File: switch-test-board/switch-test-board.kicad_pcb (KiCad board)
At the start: 4 copper layers, 1 part, among them U1 RPI4CM

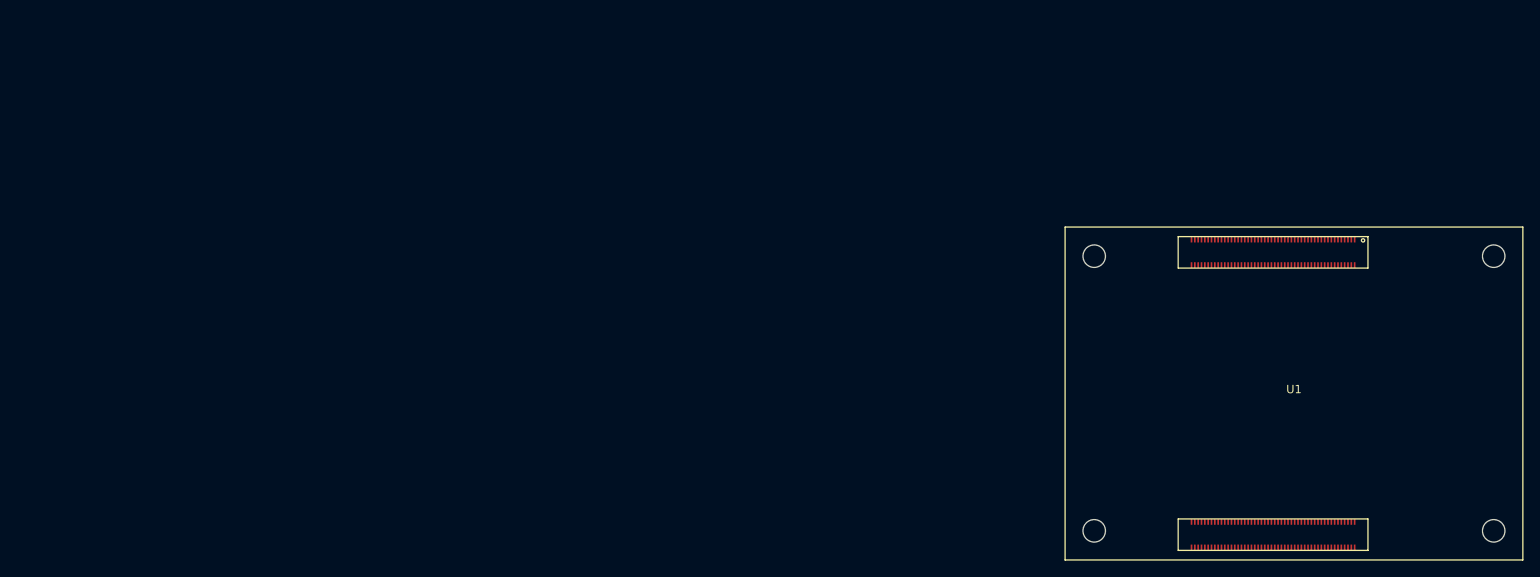
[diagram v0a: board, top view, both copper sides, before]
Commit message: Added KSZ Switch IC Decoupling and Port Leds.
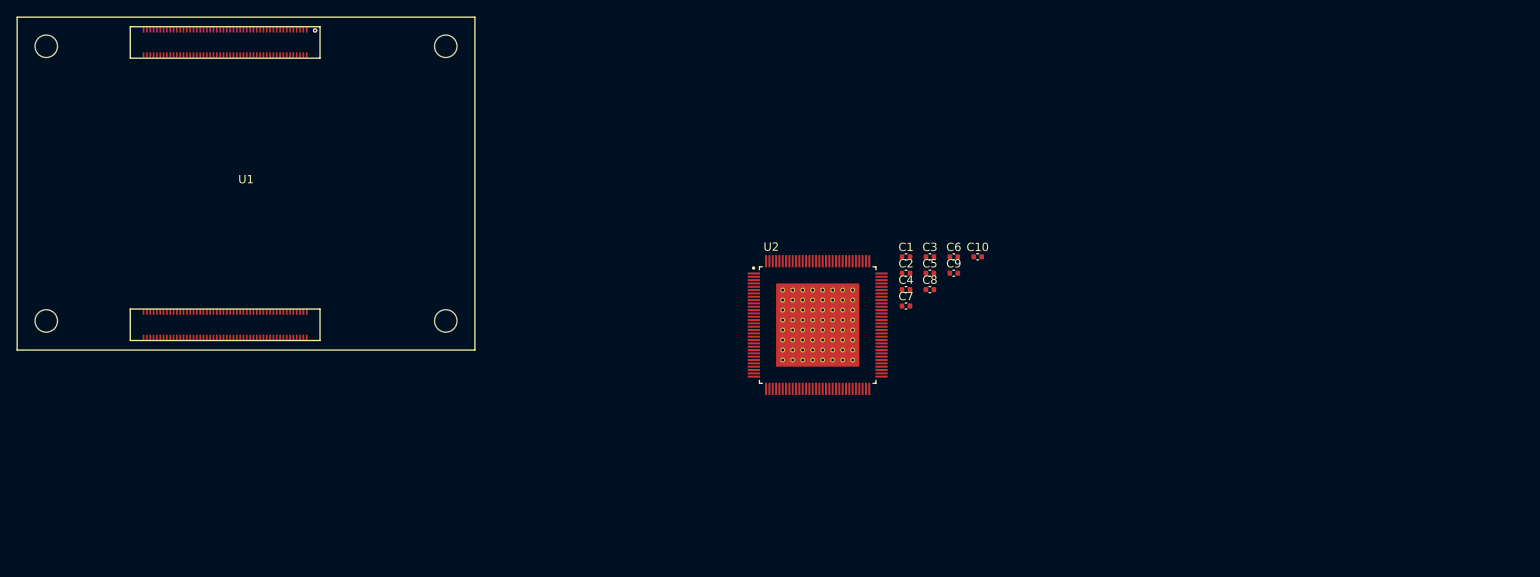
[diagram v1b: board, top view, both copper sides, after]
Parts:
- added C1: 1uF, Capacitor_SMD:C_0402_1005Metric, F.Cu at (153.4, 59.3)
- added C10: 0.1uF, Capacitor_SMD:C_0402_1005Metric, F.Cu at (162.0, 59.3)
- added C2: 0.1uF, Capacitor_SMD:C_0402_1005Metric, F.Cu at (153.4, 61.3)
- added C3: 0.1uF, Capacitor_SMD:C_0402_1005Metric, F.Cu at (156.3, 59.3)
- added C4: 0.1uF, Capacitor_SMD:C_0402_1005Metric, F.Cu at (153.4, 63.2)
- added C5: 0.1uF, Capacitor_SMD:C_0402_1005Metric, F.Cu at (156.3, 61.3)
- added C6: 0.1uF, Capacitor_SMD:C_0402_1005Metric, F.Cu at (159.1, 59.3)
- added C7: 0.1uF, Capacitor_SMD:C_0402_1005Metric, F.Cu at (153.4, 65.2)
- added C8: 0.1uF, Capacitor_SMD:C_0402_1005Metric, F.Cu at (156.3, 63.2)
- added C9: 0.1uF, Capacitor_SMD:C_0402_1005Metric, F.Cu at (159.1, 61.3)
- added U2: KSZ9477S, kicad-lib:128-TQFP-EP, F.Cu at (142.8, 67.5)
- moved U1 128.4 mm to (46.6, 70.5)
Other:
- net class Default: clearance 0.2 -> 0.15
- rule pad_to_mask_clearance: 0 -> 0.07
- rule trace_clearance: 0.2 -> 0.15

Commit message: Updated Schematic.
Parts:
- added C1: 15pF, Capacitor_SMD:C_0402_1005Metric, F.Cu at (132.6, 63.8)
- added C10: 10uF, Capacitor_SMD:C_0603_1608Metric, F.Cu at (150.5, 49.6)
- added C12: 1uF, Capacitor_SMD:C_0402_1005Metric, F.Cu at (160.3, 52.5)
- added C14: 0.1uF, Capacitor_SMD:C_0402_1005Metric, F.Cu at (123.9, 59.8)
- added C16: 0.1uF, Capacitor_SMD:C_0402_1005Metric, F.Cu at (149.8, 61.8)
- added C18: 0.1uF, Capacitor_SMD:C_0402_1005Metric, F.Cu at (157.4, 54.5)
- added C19: 0.1uF, Capacitor_SMD:C_0402_1005Metric, F.Cu at (173.3, 38.2)
- added C2: 15pF, Capacitor_SMD:C_0402_1005Metric, F.Cu at (153.1, 55.8)
- added C21: 0.1uF, Capacitor_SMD:C_0402_1005Metric, F.Cu at (146.9, 64.1)
- added C22: 0.1uF, Capacitor_SMD:C_0402_1005Metric, F.Cu at (151.2, 59.8)
- added C24: 0.1uF, Capacitor_SMD:C_0402_1005Metric, F.Cu at (161.8, 49.4)
- added C25: 0.1uF, Capacitor_SMD:C_0402_1005Metric, F.Cu at (157.4, 52.5)
- added C27: 0.1uF, Capacitor_SMD:C_0402_1005Metric, F.Cu at (153.1, 57.8)
- added C28: 0.1uF, Capacitor_SMD:C_0402_1005Metric, F.Cu at (146.9, 62.2)
- added C3: 10uF, Capacitor_SMD:C_0603_1608Metric, F.Cu at (146.5, 49.6)
- added C30: 0.1uF, Capacitor_SMD:C_0402_1005Metric, F.Cu at (173.3, 36.2)
- added C31: 0.1uF, Capacitor_SMD:C_0402_1005Metric, F.Cu at (125.6, 64.2)
- added C33: 0.1uF, Capacitor_SMD:C_0402_1005Metric, F.Cu at (138.3, 62.2)
- added C34: 0.1uF, Capacitor_SMD:C_0402_1005Metric, F.Cu at (122.7, 64.2)
- added C36: 0.1uF, Capacitor_SMD:C_0402_1005Metric, F.Cu at (144.1, 64.1)
- added C37: 0.1uF, Capacitor_SMD:C_0402_1005Metric, F.Cu at (141.2, 64.1)
- added C38: 0.1uF, Capacitor_SMD:C_0402_1005Metric, F.Cu at (138.3, 64.1)
- added C39: 0.1uF, Capacitor_SMD:C_0402_1005Metric, F.Cu at (135.5, 64.1)
- added C4: 10uF, Capacitor_SMD:C_0603_1608Metric, F.Cu at (142.4, 49.6)
- added C40: 0.1uF, Capacitor_SMD:C_0402_1005Metric, F.Cu at (144.1, 62.2)
- added C41: 0.1uF, Capacitor_SMD:C_0402_1005Metric, F.Cu at (141.2, 62.2)
- added C42: 0.1uF, Capacitor_SMD:C_0402_1005Metric, F.Cu at (129.7, 63.8)
- added C43: 0.1uF, Capacitor_SMD:C_0402_1005Metric, F.Cu at (135.5, 62.2)
- added C44: 0.1uF, Capacitor_SMD:C_0402_1005Metric, F.Cu at (148.3, 59.8)
- added C45: 10uF, Capacitor_SMD:C_0603_1608Metric, F.Cu at (168.5, 74.7)
- added C46: 0.1uF, Capacitor_SMD:C_0402_1005Metric, F.Cu at (179.0, 74.4)
- added C47: 10uF, Capacitor_SMD:C_0603_1608Metric, F.Cu at (168.5, 77.2)
- added C48: 0.1uF, Capacitor_SMD:C_0402_1005Metric, F.Cu at (178.4, 77.5)
- added C49: 10uF, Capacitor_SMD:C_0603_1608Metric, F.Cu at (172.5, 74.7)
- added C5: 10uF, Capacitor_SMD:C_0603_1608Metric, F.Cu at (130.4, 52.2)
- added C50: 0.1uF, Capacitor_SMD:C_0402_1005Metric, F.Cu at (177.3, 79.5)
- added C6: 10uF, Capacitor_SMD:C_0603_1608Metric, F.Cu at (126.3, 54.8)
- added C7: 10uF, Capacitor_SMD:C_0603_1608Metric, F.Cu at (134.4, 49.6)
- added C8: 10uF, Capacitor_SMD:C_0603_1608Metric, F.Cu at (138.4, 49.6)
- added C9: 10uF, Capacitor_SMD:C_0603_1608Metric, F.Cu at (154.5, 49.6)
- added D1: 150060GS75000, LED_SMD:LED_0603_1608Metric, F.Cu at (126.4, 49.7)
- added D10: 150060RS75000, LED_SMD:LED_0603_1608Metric, F.Cu at (173.9, 31.4)
- added D2: 150060GS75000, LED_SMD:LED_0603_1608Metric, F.Cu at (115.2, 63.3)
- added D3: 150060GS75000, LED_SMD:LED_0603_1608Metric, F.Cu at (119.3, 63.3)
- added D4: 150060GS75000, LED_SMD:LED_0603_1608Metric, F.Cu at (124.5, 57.5)
- added D5: 150060GS75000, LED_SMD:LED_0603_1608Metric, F.Cu at (120.5, 60.1)
- added D6: 150060RS75000, LED_SMD:LED_0603_1608Metric, F.Cu at (120.5, 57.5)
- added D7: 150060RS75000, LED_SMD:LED_0603_1608Metric, F.Cu at (173.9, 33.9)
- added D8: 150060RS75000, LED_SMD:LED_0603_1608Metric, F.Cu at (126.4, 52.2)
- added D9: 150060RS75000, LED_SMD:LED_0603_1608Metric, F.Cu at (130.4, 49.7)
- added FB1: BLM18EG221SN1D, kicad-lib:ferrite-blm18, F.Cu at (134.2, 52.0)
- added FB2: BLM18EG221SN1D, kicad-lib:ferrite-blm18, F.Cu at (137.8, 52.0)
- added FB3: BLM18EG221SN1D, kicad-lib:ferrite-blm18, F.Cu at (141.3, 52.0)
- added FB4: BLM18EG221SN1D, kicad-lib:ferrite-blm18, F.Cu at (144.8, 52.0)
- added FB5: BLM18EG221SN1D, kicad-lib:ferrite-blm18, F.Cu at (148.4, 52.0)
- added FB6: BLM18EG221SN1D, kicad-lib:ferrite-blm18, F.Cu at (168.3, 79.6)
- added FB7: BLM18EG221SN1D, kicad-lib:ferrite-blm18, F.Cu at (172.3, 77.1)
- added J1: 1367073-1, kicad-lib:SFP_with_Cage, F.Cu at (162.9, 39.2)
- added J3: 2011-2X10G00SD025B, Connector_PinHeader_2.54mm:PinHeader_2x10_P2.54mm_Vertical, F.Cu at (167.0, 32.4)
- added R1: 6.04K %1, Resistor_SMD:R_0402_1005Metric, F.Cu at (138.5, 56.2)
- added R10: 10K_DNP, Resistor_SMD:R_0402_1005Metric, F.Cu at (133.8, 58.2)
- added R11: 4.7K, Resistor_SMD:R_0402_1005Metric, F.Cu at (136.7, 58.2)
- added R12: 10K, Resistor_SMD:R_0402_1005Metric, F.Cu at (139.6, 58.2)
- added R13: 10K, Resistor_SMD:R_0402_1005Metric, F.Cu at (142.5, 58.2)
- added R14: 10K, Resistor_SMD:R_0402_1005Metric, F.Cu at (145.4, 58.2)
- added R15: 10K, Resistor_SMD:R_0402_1005Metric, F.Cu at (133.8, 60.2)
- added R16: 10K, Resistor_SMD:R_0402_1005Metric, F.Cu at (151.6, 51.9)
- added R17: 1K, Resistor_SMD:R_0402_1005Metric, F.Cu at (150.2, 55.9)
- added R18: 1K, Resistor_SMD:R_0402_1005Metric, F.Cu at (154.5, 51.9)
- added R19: 1K, Resistor_SMD:R_0402_1005Metric, F.Cu at (151.6, 53.9)
- added R2: 191 %1, Resistor_SMD:R_0402_1005Metric, F.Cu at (141.4, 56.2)
- added R20: 1K, Resistor_SMD:R_0402_1005Metric, F.Cu at (154.5, 53.9)
- added R21: 1K, Resistor_SMD:R_0402_1005Metric, F.Cu at (129.8, 55.9)
- added R22: 1K, Resistor_SMD:R_0402_1005Metric, F.Cu at (132.7, 54.5)
- added R23: 1K, Resistor_SMD:R_0402_1005Metric, F.Cu at (135.6, 54.2)
- added R24: 1K, Resistor_SMD:R_0402_1005Metric, F.Cu at (138.5, 54.2)
- added R25: 1K, Resistor_SMD:R_0402_1005Metric, F.Cu at (141.4, 54.2)
- added R26: 1K, Resistor_SMD:R_0402_1005Metric, F.Cu at (129.8, 61.8)
- added R27: 4.7K, Resistor_SMD:R_0402_1005Metric, F.Cu at (130.9, 57.8)
- added R28: 750R, Resistor_SMD:R_0402_1005Metric, F.Cu at (135.6, 56.2)
- added R29: 750R, Resistor_SMD:R_0402_1005Metric, F.Cu at (126.8, 62.2)
- added R3: 22R, Resistor_SMD:R_0402_1005Metric, F.Cu at (144.3, 56.2)
- added R30: 750R, Resistor_SMD:R_0402_1005Metric, F.Cu at (126.8, 60.2)
- added R31: 750R, Resistor_SMD:R_0402_1005Metric, F.Cu at (139.6, 60.2)
- added R32: 750R, Resistor_SMD:R_0402_1005Metric, F.Cu at (142.5, 60.2)
- added R33: 750R, Resistor_SMD:R_0402_1005Metric, F.Cu at (145.4, 60.2)
- added R34: 750R, Resistor_SMD:R_0402_1005Metric, F.Cu at (123.9, 62.2)
- added R35: 22R, Resistor_SMD:R_0402_1005Metric, F.Cu at (147.2, 54.2)
- added R36: 1K, Resistor_SMD:R_0402_1005Metric, F.Cu at (171.5, 79.5)
- added R37: 10K, Resistor_SMD:R_0402_1005Metric, F.Cu at (175.5, 77.5)
- added R38: 10K, Resistor_SMD:R_0402_1005Metric, F.Cu at (174.4, 79.5)
- added R4: 22R, Resistor_SMD:R_0402_1005Metric, F.Cu at (147.2, 56.2)
- added R5: 22R, Resistor_SMD:R_0402_1005Metric, F.Cu at (136.7, 60.2)
- added R6: 22R, Resistor_SMD:R_0402_1005Metric, F.Cu at (150.2, 57.8)
- added R7: 22R, Resistor_SMD:R_0402_1005Metric, F.Cu at (128.0, 58.2)
- added R8: 22R, Resistor_SMD:R_0402_1005Metric, F.Cu at (144.3, 54.2)
- added R9: 22R, Resistor_SMD:R_0402_1005Metric, F.Cu at (130.9, 59.8)
- added SW1: PTS645SM43SMTR92 LFS, Button_Switch_SMD:SW_SPST_PTS645, F.Cu at (113.0, 52.3)
- added TP1: TestPoint_Small, TestPoint:TestPoint_Pad_D1.0mm, F.Cu at (176.0, 75.0)
- added U3: MIC826TYMT, Package_DFN_QFN:MLF-6-1EP_1.6x1.6mm_P0.5mm_EP0.5x1.26mm, F.Cu at (158.4, 49.9)
- added Y1: ABM8G-25.000MHZ-B4Y-T, Crystal:Crystal_SMD_Abracon_ABM8G-4Pin_3.2x2.5mm, F.Cu at (115.8, 59.8)
- moved C15 20.3 mm to (147.2, 77.5)
- moved C20 20.3 mm to (147.2, 79.5)
- moved C29 20.3 mm to (147.2, 81.4)
- moved C11 20.3 mm to (144.3, 77.5)
- moved C23 20.3 mm to (150.0, 77.5)
- moved C26 20.3 mm to (144.3, 83.4)
- moved C35 20.3 mm to (152.9, 77.5)
- moved C13 20.3 mm to (144.3, 79.5)
- moved C17 20.3 mm to (144.3, 81.4)
- moved C32 20.3 mm to (150.0, 79.5)
- moved U2 20.3 mm to (133.7, 85.7)
- renumbered C1 to C11, C2 to C13, C3 to C15, C4 to C17, C5 to C20, C6 to C23, C7 to C26, C8 to C29, C9 to C32, C10 to C35
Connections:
- net /VDDIO_3V3 renamed +3V3
- net Net-(U2-Pad101) renamed /SCLK
- net Net-(U2-Pad12) renamed /P2_TXRX_A_P
- net Net-(U2-Pad13) renamed /P2_TXRX_A_M
- net Net-(U2-Pad15) renamed /P2_TXRX_B_P
- net Net-(U2-Pad16) renamed /P2_TXRX_B_M
- net Net-(U2-Pad17) renamed /P2_TXRX_C_P
- net Net-(U2-Pad18) renamed /P2_TXRX_C_M
- net Net-(U2-Pad20) renamed /P2_TXRX_D_P
- net Net-(U2-Pad21) renamed /P2_TXRX_D_M
- net Net-(U2-Pad48) renamed /GTXCK
- net Net-(U2-Pad49) renamed /GTXCTL
- net Net-(U2-Pad52) renamed /GTXD3
- net Net-(U2-Pad53) renamed /GTXD2
- net Net-(U2-Pad54) renamed /GTXD1
- net Net-(U2-Pad55) renamed /GTXD0
- net Net-(U2-Pad93) renamed /PME_N
- net Net-(U2-Pad94) renamed /INTRP_N
- C11 pad 1: Net-(C1-Pad1) (its old number) -> /AVDDL_1V2
- C11 pad 2: Net-(C1-Pad2) -> GND
- C13 pad 1: Net-(C2-Pad1) (its old number) -> /AVDDL_1V2
- C13 pad 2: Net-(C2-Pad2) -> GND
- C15 pad 1: Net-(C3-Pad1) -> /AVDDL_1V2
- C15 pad 2: Net-(C3-Pad2) -> GND
- C17 pad 1: Net-(C4-Pad1) -> /AVDDL_1V2
- C17 pad 2: Net-(C4-Pad2) -> GND
- C20 pad 1: Net-(C5-Pad1) -> /AVDDL_1V2
- C20 pad 2: Net-(C5-Pad2) -> GND
- C23 pad 1: Net-(C6-Pad1) -> /AVDDL_1V2
- C23 pad 2: Net-(C6-Pad2) -> GND
- C26 pad 1: Net-(C7-Pad1) -> /AVDDL_1V2
- C26 pad 2: Net-(C7-Pad2) -> GND
- C29 pad 1: Net-(C8-Pad1) -> /AVDDL_1V2
- C29 pad 2: Net-(C8-Pad2) -> GND
- C32 pad 1: Net-(C9-Pad1) -> /AVDDL_1V2
- C32 pad 2: Net-(C9-Pad2) -> GND
- C35 pad 1: Net-(C10-Pad1) -> /AVDDL_1V2
- C35 pad 2: Net-(C10-Pad2) -> GND
- U2 pad 1: Net-(U2-Pad1) -> /P1_TXRX_A_P
- U2 pad 100: Net-(U2-Pad100) -> /SCS
- U2 pad 102: Net-(U2-Pad102) -> /LED5_0
- U2 pad 103: Net-(U2-Pad103) -> /LED5_1
- U2 pad 105: Net-(U2-Pad105) -> /LED1_0
- U2 pad 106: Net-(U2-Pad106) -> /LED1_1
- U2 pad 2: Net-(U2-Pad2) -> /P1_TXRX_A_M
- U2 pad 24: Net-(U2-Pad24) -> /P1_TXRX_A_M
- U2 pad 25: Net-(U2-Pad25) -> /P1_TXRX_A_P
- U2 pad 26: Net-(U2-Pad26) -> /P1_TXRX_B_P
- U2 pad 27: Net-(U2-Pad27) -> /P1_TXRX_B_M
- U2 pad 28: Net-(U2-Pad28) -> /P1_TXRX_C_P
- U2 pad 29: Net-(U2-Pad29) -> /P1_TXRX_C_M
- U2 pad 31: Net-(U2-Pad31) -> /P1_TXRX_D_P
- U2 pad 32: Net-(U2-Pad32) -> /P1_TXRX_D_M
- U2 pad 4: Net-(U2-Pad4) -> /P1_TXRX_B_P
- U2 pad 5: Net-(U2-Pad5) -> /P1_TXRX_B_M
- U2 pad 6: Net-(U2-Pad6) -> /P1_TXRX_C_P
- U2 pad 67: Net-(U2-Pad67) -> /IBA_EN
- U2 pad 7: Net-(U2-Pad7) -> /P1_TXRX_C_M
- U2 pad 78: Net-(U2-Pad78) -> /S_TX7_M
- U2 pad 79: Net-(U2-Pad79) -> /S_TX7_P
- U2 pad 8: Net-(U2-Pad8) -> /P1_TXRX_D_P
- U2 pad 81: Net-(U2-Pad81) -> /S_RX7_P
- U2 pad 82: Net-(U2-Pad82) -> /S_RX7_M
- U2 pad 85: Net-(U2-Pad85) -> /LED4_0
- U2 pad 86: Net-(U2-Pad86) -> /LED4_1
- U2 pad 88: Net-(U2-Pad88) -> /LED3_0
- U2 pad 89: Net-(U2-Pad89) -> /LED3_1
- U2 pad 9: Net-(U2-Pad9) -> /P1_TXRX_D_M
- U2 pad 91: Net-(U2-Pad91) -> /LED2_0
- U2 pad 92: Net-(U2-Pad92) -> /LED2_1
- U2 pad 96: Net-(U2-Pad96) -> /SW_RESETN
- U2 pad 97: Net-(U2-Pad97) -> /MISO
- U2 pad 98: Net-(U2-Pad98) -> /MOSI

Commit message: PCB Design planning.
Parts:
- added C10: 0.1uF, Capacitor_SMD:C_0402_1005Metric, F.Cu at (49.2, 24.9)
- added C11: 0.1uF, Capacitor_SMD:C_0402_1005Metric, F.Cu at (49.2, 27.2)
- added C12: 0.1uF, Capacitor_SMD:C_0402_1005Metric, F.Cu at (49.0, 29.6)
- added C13: 0.1uF, Capacitor_SMD:C_0402_1005Metric, F.Cu at (49.1, 32.9)
- added C14: 0.1uF, Capacitor_SMD:C_0402_1005Metric, F.Cu at (47.0, 40.5)
- added C15: 0.1uF, Capacitor_SMD:C_0402_1005Metric, F.Cu at (47.2, 42.9)
- added C16: 0.1uF, Capacitor_SMD:C_0402_1005Metric, F.Cu at (47.2, 45.2)
- added C17: 0.1uF, Capacitor_SMD:C_0402_1005Metric, F.Cu at (47.1, 47.6)
- added C18: 0.1uF, Capacitor_SMD:C_0402_1005Metric, F.Cu at (59.1, 40.9)
- added C19: 0.1uF, Capacitor_SMD:C_0402_1005Metric, F.Cu at (59.2, 43.3)
- added C2: 10uF, Capacitor_SMD:C_0603_1608Metric, F.Cu at (62.7, 104.0)
- added C20: 0.1uF, Capacitor_SMD:C_0402_1005Metric, F.Cu at (58.9, 46.1)
- added C21: 0.1uF, Capacitor_SMD:C_0402_1005Metric, F.Cu at (58.8, 48.9)
- added C23: 0.1uF, Capacitor_SMD:C_0402_1005Metric, F.Cu at (52.2, 23.7)
- added C24: 0.1uF, Capacitor_SMD:C_0402_1005Metric, F.Cu at (51.8, 26.2)
- added C25: 0.1uF, Capacitor_SMD:C_0402_1005Metric, F.Cu at (52.1, 28.5)
- added C26: 0.1uF, Capacitor_SMD:C_0402_1005Metric, F.Cu at (51.8, 31.0)
- added C27: 0.1uF, Capacitor_SMD:C_0402_1005Metric, F.Cu at (50.0, 38.8)
- added C28: 0.1uF, Capacitor_SMD:C_0402_1005Metric, F.Cu at (49.8, 41.4)
- added C29: 0.1uF, Capacitor_SMD:C_0402_1005Metric, F.Cu at (49.7, 43.8)
- added C30: 0.1uF, Capacitor_SMD:C_0402_1005Metric, F.Cu at (49.7, 46.4)
- added C31: 0.1uF, Capacitor_SMD:C_0402_1005Metric, F.Cu at (61.7, 39.2)
- added C32: 0.1uF, Capacitor_SMD:C_0402_1005Metric, F.Cu at (62.2, 42.0)
- added C33: 0.1uF, Capacitor_SMD:C_0402_1005Metric, F.Cu at (61.6, 44.5)
- added C34: 0.1uF, Capacitor_SMD:C_0402_1005Metric, F.Cu at (61.6, 47.1)
- added C38: 10uF, Capacitor_SMD:C_0603_1608Metric, F.Cu at (63.4, -5.13)
- added C39: 10uF, Capacitor_SMD:C_0603_1608Metric, F.Cu at (114.8, -17.4)
- added C4: 10uF, Capacitor_SMD:C_0603_1608Metric, F.Cu at (65.6, 104.1)
- added C41: 10uF, Capacitor_SMD:C_0603_1608Metric, F.Cu at (146.3, 24.0)
- added C43: 10uF, Capacitor_SMD:C_0603_1608Metric, F.Cu at (149.4, 24.0)
- added C44: 10uF, Capacitor_SMD:C_0603_1608Metric, F.Cu at (152.5, 24.0)
- added C47: 10uF, Capacitor_SMD:C_0603_1608Metric, F.Cu at (155.6, 23.9)
- added C48: 10uF, Capacitor_SMD:C_0603_1608Metric, F.Cu at (112.5, -7.60)
- added C49: 0.1uF, Capacitor_SMD:C_0402_1005Metric, F.Cu at (68.8, 2.48)
- added C5: 10uF, Capacitor_SMD:C_0603_1608Metric, F.Cu at (68.4, 104.0)
- added C50: 10uF, Capacitor_SMD:C_0603_1608Metric, F.Cu at (68.4, -0.26)
- added C51: 10uF, Capacitor_SMD:C_0603_1608Metric, F.Cu at (112.5, -5.09)
- added C54: 10uF, Capacitor_SMD:C_0603_1608Metric, F.Cu at (64.9, -0.09)
- added C55: 10uF, Capacitor_SMD:C_0603_1608Metric, F.Cu at (92.5, -5.36)
- added C56: 10uF, Capacitor_SMD:C_0603_1608Metric, F.Cu at (77.2, -5.26)
- added C6: 10uF, Capacitor_SMD:C_0603_1608Metric, F.Cu at (70.4, 103.9)
- added C65: 0.1uF, Capacitor_SMD:C_0402_1005Metric, F.Cu at (97.7, -1.43)
- added C66: 0.1uF, Capacitor_SMD:C_0402_1005Metric, F.Cu at (80.2, 1.60)
- added C7: 10uF, Capacitor_SMD:C_0603_1608Metric, F.Cu at (72.9, 103.9)
- added C70: 10uF, Capacitor_SMD:C_0603_1608Metric, F.Cu at (99.3, -5.93)
- added C71: 10uF, Capacitor_SMD:C_0603_1608Metric, F.Cu at (82.5, -0.37)
- added C75: 10uF, Capacitor_SMD:C_0603_1608Metric, F.Cu at (102.5, -5.94)
- added C76: 10uF, Capacitor_SMD:C_0603_1608Metric, F.Cu at (78.3, -0.46)
- added D1: 150060RS75000, LED_SMD:LED_0603_1608Metric, F.Cu at (64.1, 88.3)
- added D2: 150060RS75000, LED_SMD:LED_0603_1608Metric, F.Cu at (70.2, 141.0)
- added D3: 150060GS75000, LED_SMD:LED_0603_1608Metric, F.Cu at (73.7, 140.8)
- added D4: 150060RS75000, LED_SMD:LED_0603_1608Metric, F.Cu at (77.5, 141.5)
- added D5: SMAJ5.0CA-TR, Diode_SMD:D_SMA, F.Cu at (139.8, 24.0)
- added H1: VIN+, MountingHole:MountingHole_3.2mm_M3_Pad, F.Cu at (131.9, 16.8)
- added H2: VIN-, MountingHole:MountingHole_3.2mm_M3_Pad, F.Cu at (131.9, 32.9)
- added J1: USB_B_Micro, Connector_USB:USB_Micro-B_GCT_USB3076-30-A, F.Cu at (78.8, 89.3)
- added J2: 2011-2X10G00SD025B, Connector_PinHeader_2.54mm:PinHeader_2x10_P2.54mm_Vertical, F.Cu at (78.6, 104.9)
- added R1: 2.2K, Resistor_SMD:R_0402_1005Metric, F.Cu at (72.4, 93.2)
- added R10: 0R, Resistor_SMD:R_0402_1005Metric, F.Cu at (65.6, 94.4)
- added R11: 1K, Resistor_SMD:R_0402_1005Metric, F.Cu at (70.4, 137.7)
- added R12: 1K, Resistor_SMD:R_0402_1005Metric, F.Cu at (72.8, 137.7)
- added R13: 1K, Resistor_SMD:R_0402_1005Metric, F.Cu at (76.0, 137.7)
- added R2: 2.2K_DNP, Resistor_SMD:R_0402_1005Metric, F.Cu at (72.4, 91.2)
- added R30: 56K, Resistor_SMD:R_0402_1005Metric, F.Cu at (64.1, 2.50)
- added R31: 10K, Resistor_SMD:R_0402_1005Metric, F.Cu at (66.6, 2.49)
- added R50: 24K, Resistor_SMD:R_0402_1005Metric, F.Cu at (93.1, -1.48)
- added R51: 10K, Resistor_SMD:R_0402_1005Metric, F.Cu at (95.4, -1.46)
- added R52: 40.2K, Resistor_SMD:R_0402_1005Metric, F.Cu at (75.9, 1.54)
- added R53: 10K, Resistor_SMD:R_0402_1005Metric, F.Cu at (78.1, 1.56)
- added R54: 10K, Resistor_SMD:R_0402_1005Metric, F.Cu at (108.2, 158.9)
- added R6: 4.7K, Resistor_SMD:R_0402_1005Metric, F.Cu at (210.8, 124.6)
- added R7: 4.7K, Resistor_SMD:R_0402_1005Metric, F.Cu at (213.4, 124.8)
- added R8: 1K, Resistor_SMD:R_0402_1005Metric, F.Cu at (64.2, 91.2)
- added R9: 0R_DNP, Resistor_SMD:R_0402_1005Metric, F.Cu at (62.7, 94.4)
- added TP2: TestPoint, TestPoint:TestPoint_Pad_D1.0mm, F.Cu at (76.0, -12.2)
- added TP3: TestPoint, TestPoint:TestPoint_Pad_D1.0mm, F.Cu at (70.1, -12.5)
- added TP4: TestPoint, TestPoint:TestPoint_Pad_D1.0mm, F.Cu at (73.2, -12.5)
- added TP5: TestPoint, TestPoint:TestPoint_Pad_D1.0mm, F.Cu at (67.4, -12.7)
- added TP6: TestPoint, TestPoint:TestPoint_Pad_D1.0mm, F.Cu at (79.3, -12.5)
- added TP7: TestPoint, TestPoint:TestPoint_Pad_D1.0mm, F.Cu at (116.1, 158.7)
- added TP8: TestPoint, TestPoint:TestPoint_Pad_D1.0mm, F.Cu at (113.2, 158.9)
- added U10: MDT420M02001, kicad-lib:M.2_Amphenol_MDT_2280, F.Cu at (84.3, 177.2)
- added U3: LD39200PUR, Package_DFN_QFN:DFN-6-1EP_3x3mm_P0.95mm_EP1.7x2.6mm, F.Cu at (67.1, -4.70)
- added U4: piSlice-PCIe-X1-Conn, kicad-lib:10018783-10200TLF, F.Cu at (116.1, 164.8)
- added U5: LM1085ISX-3.3/NOPB, Package_TO_SOT_SMD:TO-263-3_TabPin2, F.Cu at (123.2, -10.4)
- added U6: LD39200PUR, Package_DFN_QFN:DFN-6-1EP_3x3mm_P0.95mm_EP1.7x2.6mm, F.Cu at (95.6, -4.87)
- added U7: LD39200PUR, Package_DFN_QFN:DFN-6-1EP_3x3mm_P0.95mm_EP1.7x2.6mm, F.Cu at (80.2, -4.77)
- added U8: piSlice-PCIe-X1-Edge, kicad-lib:piSlice_PCIexpress_x1, F.Cu at (178.1, 143.2)
- moved D7 214.6 mm to (329.0, 81.9)
- moved D10 213.3 mm to (332.7, 81.2)
- moved D11 213.3 mm to (332.7, 78.6)
- moved D13 209.3 mm to (333.0, 85.2)
- moved R49 206.8 mm to (336.2, 72.0)
- moved D8 206.1 mm to (324.8, 78.9)
- moved D9 205.2 mm to (328.6, 78.6)
- moved D6 201.3 mm to (325.0, 82.2)
- moved D14 201.2 mm to (328.4, 85.5)
- moved R44 194.9 mm to (324.2, 69.8)
- moved R45 194.6 mm to (326.6, 69.8)
- moved R46 194.6 mm to (329.6, 69.6)
- moved R47 194.5 mm to (332.4, 69.5)
- moved R48 194.5 mm to (335.3, 69.5)
- moved R42 180.1 mm to (330.7, 72.7)
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- renumbered C45 to C1, C49 to C22, C46 to C3, C50 to C35, C1 to C36, C2 to C37, C3 to C40, C4 to C42, C5 to C45, C6 to C46, C7 to C52, C8 to C53, C9 to C57, C10 to C58, C11 to C59, C12 to C60, C13 to C61, C14 to C62, C15 to C63, C16 to C64, C17 to C67, C18 to C68, C19 to C69, C20 to C72, C21 to C73, C22 to C74, C23 to C77, C24 to C78, C25 to C79, C47 to C8, C26 to C80, C27 to C81, C28 to C82, C29 to C83, C30 to C84, C31 to C85, C32 to C86, C33 to C87, C34 to C88, C35 to C89, C48 to C9, C36 to C90, C37 to C91, C38 to C92, C39 to C93, C40 to C94, C41 to C95, C42 to C96, C43 to C97, C44 to C98, D5 to D10, D6 to D11, D7 to D12, D8 to D13, D9 to D14, D10 to D15, D1 to D6, D2 to D7, D3 to D8, D4 to D9, FB6 to FB1, FB7 to FB2, FB1 to FB3, FB2 to FB4, FB3 to FB5, FB4 to FB6, FB5 to FB7, J1 to J3, J3 to J4, R1 to R14, R2 to R15, R3 to R16, R4 to R17, R5 to R18, R6 to R19, R7 to R20, R8 to R21, R9 to R22, R10 to R23, R11 to R24, R12 to R25, R13 to R26, R14 to R27, R15 to R28, R16 to R29, R36 to R3, R27 to R32, R28 to R33, R29 to R34, R30 to R35, R31 to R36, R32 to R37, R33 to R38, R34 to R39, R37 to R4, R17 to R40, R18 to R41, R19 to R42, R20 to R43, R21 to R44, R22 to R45, R23 to R46, R24 to R47, R25 to R48, R26 to R49, R38 to R5, R35 to R55, U3 to U9
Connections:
- U1 pad 1: Net-(U1-Pad1) -> GND
- U1 pad 10: Net-(U1-Pad10) -> /RPI_ETH_P0_N
- U1 pad 100: Net-(U1-Pad100) -> /nEXTRST
- U1 pad 101: Net-(U1-Pad101) -> /RPI_USB_ID
- U1 pad 102: Net-(U1-Pad102) -> /RPI_PCIe_CLK_nREQ
- U1 pad 103: Net-(U1-Pad103) -> /RPI_USB_DM
- U1 pad 105: Net-(U1-Pad105) -> /RPI_USB_DP
- U1 pad 107: Net-(U1-Pad107) -> GND
- U1 pad 108: Net-(U1-Pad108) -> GND
- U1 pad 109: Net-(U1-Pad109) -> /RPI_PCIe_nRST
- U1 pad 11: Net-(U1-Pad11) -> /RPI_ETH_P2_P
- U1 pad 110: Net-(U1-Pad110) -> /RPI_PCIe_CLK_P
- U1 pad 112: Net-(U1-Pad112) -> /RPI_PCIe_CLK_N
- U1 pad 113: Net-(U1-Pad113) -> GND
- U1 pad 114: Net-(U1-Pad114) -> GND
- U1 pad 116: Net-(U1-Pad116) -> /RPI_PCIe_RX_P
- U1 pad 118: Net-(U1-Pad118) -> /RPI_PCIe_RX_N
- U1 pad 119: Net-(U1-Pad119) -> GND
- U1 pad 12: Net-(U1-Pad12) -> /RPI_ETH_P0_P
- U1 pad 120: Net-(U1-Pad120) -> GND
- U1 pad 122: Net-(U1-Pad122) -> /RPI_PCIe_TX_P
- U1 pad 124: Net-(U1-Pad124) -> /RPI_PCIe_TX_N
- U1 pad 125: Net-(U1-Pad125) -> GND
- U1 pad 126: Net-(U1-Pad126) -> GND
- U1 pad 13: Net-(U1-Pad13) -> GND
- U1 pad 131: Net-(U1-Pad131) -> GND
- U1 pad 132: Net-(U1-Pad132) -> GND
- U1 pad 137: Net-(U1-Pad137) -> GND
- U1 pad 138: Net-(U1-Pad138) -> GND
- U1 pad 14: Net-(U1-Pad14) -> GND
- U1 pad 144: Net-(U1-Pad144) -> GND
- U1 pad 15: Net-(U1-Pad15) -> /RPI_ETH_LED3
- U1 pad 150: Net-(U1-Pad150) -> GND
- U1 pad 155: Net-(U1-Pad155) -> GND
- U1 pad 156: Net-(U1-Pad156) -> GND
- U1 pad 161: Net-(U1-Pad161) -> GND
- U1 pad 162: Net-(U1-Pad162) -> GND
- U1 pad 167: Net-(U1-Pad167) -> GND
- U1 pad 168: Net-(U1-Pad168) -> GND
- U1 pad 17: Net-(U1-Pad17) -> /RPI_ETH_LED2
- U1 pad 173: Net-(U1-Pad173) -> GND
- U1 pad 174: Net-(U1-Pad174) -> GND
- U1 pad 179: Net-(U1-Pad179) -> GND
- U1 pad 180: Net-(U1-Pad180) -> GND
- U1 pad 185: Net-(U1-Pad185) -> GND
- U1 pad 186: Net-(U1-Pad186) -> GND
- U1 pad 19: Net-(U1-Pad19) -> /RPI_ETH_LED1
- U1 pad 191: Net-(U1-Pad191) -> GND
- U1 pad 192: Net-(U1-Pad192) -> GND
- U1 pad 197: Net-(U1-Pad197) -> GND
- U1 pad 198: Net-(U1-Pad198) -> GND
- U1 pad 2: Net-(U1-Pad2) -> GND
- U1 pad 20: Net-(U1-Pad20) -> /EEPROM_nWP
- U1 pad 21: Net-(U1-Pad21) -> /LED_Activity
- U1 pad 22: Net-(U1-Pad22) -> GND
- U1 pad 23: Net-(U1-Pad23) -> GND
- U1 pad 25: Net-(U1-Pad25) -> /SCLK
- U1 pad 26: Net-(U1-Pad26) -> /MISO
- U1 pad 27: Net-(U1-Pad27) -> /MOSI
- U1 pad 3: Net-(U1-Pad3) -> /RPI_ETH_P3_P
- U1 pad 32: Net-(U1-Pad32) -> GND
- U1 pad 33: Net-(U1-Pad33) -> GND
- U1 pad 4: Net-(U1-Pad4) -> /RPI_ETH_P1_P
- U1 pad 42: Net-(U1-Pad42) -> GND
- U1 pad 43: Net-(U1-Pad43) -> GND
- U1 pad 49: Net-(U1-Pad49) -> /SCS
- U1 pad 5: Net-(U1-Pad5) -> /RPI_ETH_P3_N
- U1 pad 51: Net-(U1-Pad51) -> /RPI_UART_TX
- U1 pad 52: Net-(U1-Pad52) -> GND
- U1 pad 53: Net-(U1-Pad53) -> GND
- U1 pad 55: Net-(U1-Pad55) -> /RPI_UART_RX
- U1 pad 57: Net-(U1-Pad57) -> (no net)
- U1 pad 58: Net-(U1-Pad58) -> /KSZ_RESETN
- U1 pad 59: Net-(U1-Pad59) -> GND
- U1 pad 6: Net-(U1-Pad6) -> /RPI_ETH_P1_N
- U1 pad 60: Net-(U1-Pad60) -> GND
- U1 pad 61: Net-(U1-Pad61) -> (no net)
- U1 pad 62: Net-(U1-Pad62) -> (no net)
- U1 pad 63: Net-(U1-Pad63) -> (no net)
- U1 pad 64: Net-(U1-Pad64) -> (no net)
- U1 pad 65: Net-(U1-Pad65) -> GND
- U1 pad 66: Net-(U1-Pad66) -> GND
- U1 pad 67: Net-(U1-Pad67) -> (no net)
- U1 pad 68: Net-(U1-Pad68) -> (no net)
- U1 pad 69: Net-(U1-Pad69) -> (no net)
- U1 pad 7: Net-(U1-Pad7) -> GND
- U1 pad 70: Net-(U1-Pad70) -> (no net)
- U1 pad 71: Net-(U1-Pad71) -> GND
- U1 pad 72: Net-(U1-Pad72) -> (no net)
- U1 pad 73: Net-(U1-Pad73) -> (no net)
- U1 pad 74: Net-(U1-Pad74) -> GND
- U1 pad 75: Net-(U1-Pad75) -> (no net)
- U1 pad 77: Net-(U1-Pad77) -> +5V
- U1 pad 79: Net-(U1-Pad79) -> +5V
- U1 pad 8: Net-(U1-Pad8) -> GND
- U1 pad 80: Net-(U1-Pad80) -> /SFP_I2C_SCL
- U1 pad 81: Net-(U1-Pad81) -> +5V
- U1 pad 82: Net-(U1-Pad82) -> /SFP_I2C_SDA
- U1 pad 83: Net-(U1-Pad83) -> +5V
- U1 pad 84: Net-(U1-Pad84) -> /RPI_3V3
- U1 pad 85: Net-(U1-Pad85) -> +5V
- U1 pad 86: Net-(U1-Pad86) -> /RPI_3V3
- U1 pad 87: Net-(U1-Pad87) -> +5V
- U1 pad 88: Net-(U1-Pad88) -> /RPI_1V8
- U1 pad 9: Net-(U1-Pad9) -> /RPI_ETH_P2_N
- U1 pad 90: Net-(U1-Pad90) -> /RPI_1V8
- U1 pad 92: Net-(U1-Pad92) -> /RUN_PG
- U1 pad 93: Net-(U1-Pad93) -> /nRPIBOOT
- U1 pad 95: Net-(U1-Pad95) -> /LED_PWR
- U1 pad 98: Net-(U1-Pad98) -> GND
- U1 pad 99: Net-(U1-Pad99) -> /GLOBAL_EN
- U2 pad 24: /P1_TXRX_A_M -> /P3_TXRX_A_M
- U2 pad 25: /P1_TXRX_A_P -> /P3_TXRX_A_P
- U2 pad 26: /P1_TXRX_B_P -> /P3_TXRX_B_P
- U2 pad 27: /P1_TXRX_B_M -> /P3_TXRX_B_M
- U2 pad 28: /P1_TXRX_C_P -> /P3_TXRX_C_P
- U2 pad 29: /P1_TXRX_C_M -> /P3_TXRX_C_M
- U2 pad 31: /P1_TXRX_D_P -> /P3_TXRX_D_P
- U2 pad 32: /P1_TXRX_D_M -> /P3_TXRX_D_M
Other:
- board outline added: 20.3 x 8.4 mm

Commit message: PCB Design Updated.
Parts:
- moved C35 53.7 mm to (203.9, 105.7), turned to 0 degrees
- moved C22 52.6 mm to (204.4, 104.5), turned to 0 degrees
- moved C3 51.6 mm to (203.3, 100.7), turned to 0 degrees
- moved C9 50.5 mm to (201.9, 105.7), turned to 180 degrees
- moved R54 49.5 mm to (78.3, 119.4)
- moved U4 49.5 mm to (86.2, 125.3)
- moved TP7 49.5 mm to (86.2, 119.1)
- moved U10 49.5 mm to (54.4, 137.7)
- moved TP8 49.5 mm to (83.4, 119.4)
- moved R15 49.5 mm to (260.6, 78.3)
- moved R21 49.5 mm to (258.1, 88.3)
- moved R22 49.5 mm to (257.9, 85.5)
- moved R14 49.5 mm to (257.0, 78.6)
- moved R17 49.5 mm to (274.2, 78.4)
- moved R18 49.5 mm to (255.2, 88.5)
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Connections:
- net /S_RX7_M renamed /S_RX7_N
- net /S_TX7_M renamed /S_TX7_N
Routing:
- net /S_TX7_N: track 0.00 -> 35.1 mm, vias 0 -> 2
- net /S_TX7_P: track 0.00 -> 34.5 mm, vias 0 -> 2
- net /S_RX7_N: track 0.00 -> 32.4 mm, vias 0 -> 2
- net /S_RX7_P: track 0.00 -> 31.8 mm, vias 0 -> 2
- net /SFP_RATE_SEL: track 0.00 -> 12.3 mm
- net /SFP_I2C_SDA: track 0.00 -> 12.1 mm
- net /SFP_I2C_SCL: track 0.00 -> 11.7 mm
- net /SFP_TX_DIS: track 0.00 -> 10.8 mm
- net /SFP_TX_FAULT: track 0.00 -> 10.6 mm
- net GND: track 0.00 -> 10.4 mm, vias 0 -> 2
- net /SFP_LOS: track 0.00 -> 9.36 mm
- net /VCC_SFP_R: track 0.00 -> 8.24 mm
- net /VCC_SFP_T: track 0.00 -> 7.19 mm
- net +3V3: track 0.00 -> 3.79 mm
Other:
- outline, holes or cut-outs redrawn
- net class Default: clearance 0.15 -> 0.1; trace_width 0.25 -> 0.1; via_dia 0.8 -> 0.5; via_drill 0.4 -> 0.2
- net class SGMII added: clearance 0.1524, trace_width 0.11049, via_dia 0.5, via_drill 0.2
- rule trace_clearance: 0.15 -> 0.1
- rule trace_min: 0.2 -> 0.1
- rule via_min_drill: 0.3 -> 0.2

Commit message: Completed routing eth. interfaces.
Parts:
- C63, C64, C67, C69: moved to B.Cu
- moved C2 300.0 mm to (324.7, 131.2)
- moved C5 300.0 mm to (330.4, 131.1)
- moved R1 300.0 mm to (334.3, 120.3)
- moved R2 300.0 mm to (334.3, 118.3)
- moved R54 300.0 mm to (373.4, 173.4)
- moved R8 300.0 mm to (326.2, 118.4)
- moved C4 300.0 mm to (327.6, 131.2)
- moved C6 300.0 mm to (332.3, 131.0)
- moved C7 300.0 mm to (334.8, 131.0)
- moved D1 300.0 mm to (326.1, 115.5)
- moved D2 300.0 mm to (332.2, 168.2)
- moved D3 300.0 mm to (335.7, 168.0)
- moved D4 300.0 mm to (339.5, 168.6)
- moved R10 300.0 mm to (327.6, 121.6)
- moved R11 300.0 mm to (332.4, 164.9)
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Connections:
- net /P1_TXRX_A_M renamed /P1_TXRX_A_N
- net /P1_TXRX_B_M renamed /P1_TXRX_B_N
- net /P1_TXRX_C_M renamed /P1_TXRX_C_N
- net /P1_TXRX_D_M renamed /P1_TXRX_D_N
- net /P2_TXRX_A_M renamed /P2_TXRX_A_N
- net /P2_TXRX_B_M renamed /P2_TXRX_B_N
- net /P2_TXRX_C_M renamed /P2_TXRX_C_N
- net /P2_TXRX_D_M renamed /P2_TXRX_D_N
- net /P3_TXRX_B_M renamed /P3_TXRX_B_N
- net /P3_TXRX_C_M renamed /P3_TXRX_C_N
- net /P3_TXRX_D_M renamed /P3_TXRX_D_N
- C18 pad 1: /P3_TXRX_A_M -> /P3_TXRX_A_N
- U2 pad 24: /P3_TXRX_A_M -> /P3_TXRX_A_P
- U2 pad 25: /P3_TXRX_A_P -> /P3_TXRX_A_N
- U4 pad A13: /X1_CON_ETH_P3_P -> /X1_CON_ETH_P2_P
- U4 pad A14: /X1_CON_ETH_P3_N -> /X1_CON_ETH_P2_N
- U4 pad A16: /X1_CON_ETH_P2_P -> /X1_CON_ETH_P3_P
- U4 pad A17: /X1_CON_ETH_P2_N -> /X1_CON_ETH_P3_N
- U8 pad A13: /X1_EDGE_ETH_P3_P -> /X1_EDGE_ETH_P2_P
- U8 pad A14: /X1_EDGE_ETH_P3_N -> /X1_EDGE_ETH_P2_N
- U8 pad A16: /X1_EDGE_ETH_P2_P -> /X1_EDGE_ETH_P3_P
- U8 pad A17: /X1_EDGE_ETH_P2_N -> /X1_EDGE_ETH_P3_N
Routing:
- net /RPI_ETH_P1_N: track 0.00 -> 29.2 mm
- net /DVDDL_1V2: track 0.00 -> 28.4 mm, vias 0 -> 9
- net /RPI_ETH_P1_P: track 0.00 -> 28.3 mm
- net /RPI_ETH_P0_N: track 0.00 -> 26.7 mm
- net /RPI_ETH_P0_P: track 0.00 -> 26.7 mm
- net /AVDDL_1V2: track 0.00 -> 26.2 mm, vias 0 -> 8
- net GND: track 10.4 -> 36.0 mm, vias 2 -> 25
- net /RPI_ETH_P3_P: track 0.00 -> 25.0 mm, vias 0 -> 2
- net /RPI_ETH_P3_N: track 0.00 -> 24.6 mm, vias 0 -> 2
- net /RPI_ETH_P2_N: track 0.00 -> 24.1 mm, vias 0 -> 2
- net /RPI_ETH_P2_P: track 0.00 -> 24.1 mm, vias 0 -> 2
- net /AVDDH_2V5: track 0.00 -> 22.4 mm, vias 0 -> 7
- net /X1_EDGE_ETH_P2_P: track 0.00 -> 19.3 mm, vias 0 -> 1
- net /X1_EDGE_ETH_P2_N: track 0.00 -> 19.3 mm, vias 0 -> 1
- net /X1_EDGE_ETH_P0_P: track 0.00 -> 19.2 mm
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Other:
- board size 20.3 x 8.4 mm -> 100.7 x 102.7 mm
- net class ETH added: clearance 0.1524, trace_width 0.11049, via_dia 0.5, via_drill 0.2
- net class PCIe added: clearance 0.1, trace_width 0.1, via_dia 0.5, via_drill 0.2
- net class USB added: clearance 0.1, trace_width 0.1, via_dia 0.5, via_drill 0.2
